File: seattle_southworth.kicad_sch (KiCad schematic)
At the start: 20 parts

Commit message: pier 50 routing checkpoint
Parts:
- added LED1221, LED1222, LED1223: WS2812B-2020, EasyEDA:LED-SMD_4P-L2.0-W2.0-TL_WS2812B-2020, symbol EasyEDA:WS2812B-2020
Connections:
- net +VLED: now also LED1221.4 (VDD), LED1222.4 (VDD), LED1223.4 (VDD)
- net GND: now also LED1221.2 (GND), LED1222.2 (GND), LED1223.2 (GND)
- net at LED1210.1 (DO): now also LED1221.3 (DI)
- net at LED1220.1 (DO): now also LED1222.3 (DI)
- net at LED1201.3 (DI): now also LED1223.1 (DO)

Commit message: single ferry track checkpoint
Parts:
- removed LED1211, LED1212, LED1213, LED1214, LED1215, LED1216, LED1217, LED1218, LED1219, LED1220, LED1222: WS2812B-2020, EasyEDA:LED-SMD_4P-L2.0-W2.0-TL_WS2812B-2020, symbol EasyEDA:WS2812B-2020

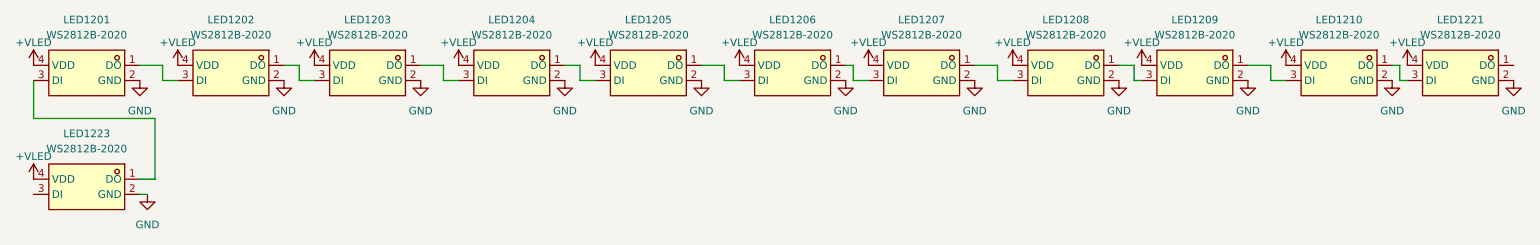
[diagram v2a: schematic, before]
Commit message: Add rail labels
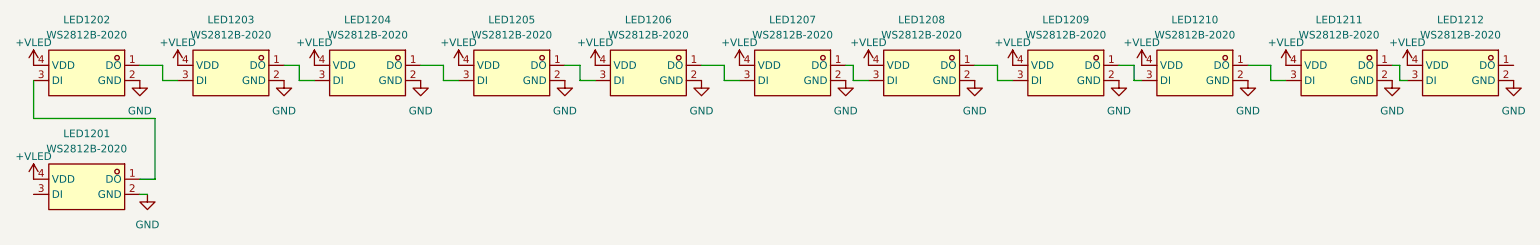
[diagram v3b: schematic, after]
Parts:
- renumbered LED1223 to LED1201, LED1201 to LED1202, LED1202 to LED1203, LED1203 to LED1204, LED1204 to LED1205, LED1205 to LED1206, LED1206 to LED1207, LED1207 to LED1208, LED1208 to LED1209, LED1209 to LED1210, LED1210 to LED1211, LED1221 to LED1212
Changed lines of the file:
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@@
 		(in_pos_files yes)
 		(dnp no)
-		(property "Reference" "LED1204"
+		(property "Reference" "LED1205"
 			(at 109.22 25.4 0)
 			(show_name no)
@@
 			(project "transit"
 				(path "/3763eade-a8c8-4ec0-9cf2-9db4442b4ee5/153adc6e-a3b0-4527-a19a-87e28aab4b4d/7c9fe608-8e01-49b2-89d0-9d6a8f9574e8"
-					(reference "LED1204")
+					(reference "LED1205")
 					(unit 1)
 				)
@@
 		(in_pos_files yes)
 		(dnp no)
-		(property "Reference" "LED1210"
+		(property "Reference" "LED1211"
 			(at 247.65 25.4 0)
 			(show_name no)
@@
 			(project "transit"
 				(path "/3763eade-a8c8-4ec0-9cf2-9db4442b4ee5/153adc6e-a3b0-4527-a19a-87e28aab4b4d/7c9fe608-8e01-49b2-89d0-9d6a8f9574e8"
-					(reference "LED1210")
+					(reference "LED1211")
 					(unit 1)
 				)
@@
 		(in_pos_files yes)
 		(dnp no)
-		(property "Reference" "LED1223"
+		(property "Reference" "LED1201"
 			(at 38.1 44.45 0)
 			(show_name no)
@@
 			(project "transit"
 				(path "/3763eade-a8c8-4ec0-9cf2-9db4442b4ee5/153adc6e-a3b0-4527-a19a-87e28aab4b4d/7c9fe608-8e01-49b2-89d0-9d6a8f9574e8"
-					(reference "LED1223")
+					(reference "LED1201")
 					(unit 1)
 				)
@@
 		(in_pos_files yes)
 		(dnp no)
-		(property "Reference" "LED1208"
+		(property "Reference" "LED1209"
 			(at 201.93 25.4 0)
 			(show_name no)
@@
 			(project "transit"
 				(path "/3763eade-a8c8-4ec0-9cf2-9db4442b4ee5/153adc6e-a3b0-4527-a19a-87e28aab4b4d/7c9fe608-8e01-49b2-89d0-9d6a8f9574e8"
-					(reference "LED1208")
+					(reference "LED1209")
 					(unit 1)
 				)
@@
 		(in_pos_files yes)
 		(dnp no)
-		(property "Reference" "LED1203"
+		(property "Reference" "LED1204"
 			(at 85.09 25.4 0)
 			(show_name no)
@@
 			(project "transit"
 				(path "/3763eade-a8c8-4ec0-9cf2-9db4442b4ee5/153adc6e-a3b0-4527-a19a-87e28aab4b4d/7c9fe608-8e01-49b2-89d0-9d6a8f9574e8"
-					(reference "LED1203")
+					(reference "LED1204")
 					(unit 1)
 				)
@@
 		(in_pos_files yes)
 		(dnp no)
-		(property "Reference" "LED1221"
+		(property "Reference" "LED1212"
 			(at 267.97 25.4 0)
 			(show_name no)
@@
 			(project "transit"
 				(path "/3763eade-a8c8-4ec0-9cf2-9db4442b4ee5/153adc6e-a3b0-4527-a19a-87e28aab4b4d/7c9fe608-8e01-49b2-89d0-9d6a8f9574e8"
-					(reference "LED1221")
+					(reference "LED1212")
 					(unit 1)
 				)
@@
 		(in_pos_files yes)
 		(dnp no)
-		(property "Reference" "LED1206"
+		(property "Reference" "LED1207"
 			(at 156.21 25.4 0)
 			(show_name no)
@@
 			(project "transit"
 				(path "/3763eade-a8c8-4ec0-9cf2-9db4442b4ee5/153adc6e-a3b0-4527-a19a-87e28aab4b4d/7c9fe608-8e01-49b2-89d0-9d6a8f9574e8"
-					(reference "LED1206")
+					(reference "LED1207")
 					(unit 1)
 				)
@@
 		(in_pos_files yes)
 		(dnp no)
-		(property "Reference" "LED1205"
+		(property "Reference" "LED1206"
 			(at 132.08 25.4 0)
 			(show_name no)
@@
 			(project "transit"
 				(path "/3763eade-a8c8-4ec0-9cf2-9db4442b4ee5/153adc6e-a3b0-4527-a19a-87e28aab4b4d/7c9fe608-8e01-49b2-89d0-9d6a8f9574e8"
-					(reference "LED1205")
+					(reference "LED1206")
 					(unit 1)
 				)
@@
 		(in_pos_files yes)
 		(dnp no)
-		(property "Reference" "LED1202"
+		(property "Reference" "LED1203"
 			(at 62.23 25.4 0)
 			(show_name no)
@@
 			(project "transit"
 				(path "/3763eade-a8c8-4ec0-9cf2-9db4442b4ee5/153adc6e-a3b0-4527-a19a-87e28aab4b4d/7c9fe608-8e01-49b2-89d0-9d6a8f9574e8"
-					(reference "LED1202")
+					(reference "LED1203")
 					(unit 1)
 				)
@@
 		(in_pos_files yes)
 		(dnp no)
-		(property "Reference" "LED1209"
+		(property "Reference" "LED1210"
 			(at 223.52 25.4 0)
 			(show_name no)
@@
 			(project "transit"
 				(path "/3763eade-a8c8-4ec0-9cf2-9db4442b4ee5/153adc6e-a3b0-4527-a19a-87e28aab4b4d/7c9fe608-8e01-49b2-89d0-9d6a8f9574e8"
-					(reference "LED1209")
+					(reference "LED1210")
 					(unit 1)
 				)
@@
 		(in_pos_files yes)
 		(dnp no)
-		(property "Reference" "LED1201"
+		(property "Reference" "LED1202"
 			(at 38.1 25.4 0)
 			(show_name no)
@@
 			(project "transit"
 				(path "/3763eade-a8c8-4ec0-9cf2-9db4442b4ee5/153adc6e-a3b0-4527-a19a-87e28aab4b4d/7c9fe608-8e01-49b2-89d0-9d6a8f9574e8"
-					(reference "LED1201")
+					(reference "LED1202")
 					(unit 1)
 				)
@@
 		(in_pos_files yes)
 		(dnp no)
-		(property "Reference" "LED1207"
+		(property "Reference" "LED1208"
 			(at 177.8 25.4 0)
 			(show_name no)
@@
 			(project "transit"
 				(path "/3763eade-a8c8-4ec0-9cf2-9db4442b4ee5/153adc6e-a3b0-4527-a19a-87e28aab4b4d/7c9fe608-8e01-49b2-89d0-9d6a8f9574e8"
-					(reference "LED1207")
-					(unit 1)
-				)
+					(reference "LED1208")
+					(unit 1)
+				)

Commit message: junction checkpoint
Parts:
- added LED1213: WS2812B-2020, EasyEDA:LED-SMD_4P-L2.0-W2.0-TL_WS2812B-2020, symbol EasyEDA:WS2812B-2020
- renumbered LED1212 to LED1201, LED1211 to LED1202, LED1210 to LED1203, LED1209 to LED1204, LED1208 to LED1205, LED1207 to LED1206, LED1206 to LED1207, LED1205 to LED1208, LED1204 to LED1209, LED1203 to LED1210, LED1202 to LED1211, LED1201 to LED1212
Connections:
- net +VLED: now also LED1213.4 (VDD)
- net GND: now also LED1213.2 (GND)
- net at LED1208.1 (DO): now also LED1209.3 (DI); no longer LED1207.3 (DI)
- net at LED1208.3 (DI): now also LED1207.1 (DO); no longer LED1209.1 (DO)
- net at LED1202.1 (DO): now also LED1203.3 (DI); no longer LED1201.3 (DI)
- net at LED1202.3 (DI): now also LED1201.1 (DO); no longer LED1203.1 (DO)
- net at LED1212.1 (DO): now also LED1213.3 (DI); no longer LED1211.3 (DI)
- net at LED1212.3 (DI): now also LED1211.1 (DO)
- net at LED1204.1 (DO): now also LED1205.3 (DI); no longer LED1203.3 (DI)
- net at LED1204.3 (DI): now also LED1203.1 (DO); no longer LED1205.1 (DO)
- net at LED1210.1 (DO): now also LED1211.3 (DI); no longer LED1209.3 (DI)
- net at LED1206.1 (DO): now also LED1207.3 (DI); no longer LED1205.3 (DI)
- net at LED1206.3 (DI): now also LED1205.1 (DO); no longer LED1207.1 (DO)
- net at LED1210.3 (DI): now also LED1209.1 (DO); no longer LED1211.1 (DO)
- new net WATER_TAXI_SOUTHWORTH: LED1201.3 (DI)
- new net WT_FERRY_MERGE: LED1213.1 (DO)
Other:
- moved on the sheet: LED1201, LED1202, LED1203, LED1204, LED1205, LED1206, LED1207, LED1208, LED1209, LED1210, LED1211, LED1212

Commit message: rev-b validation run
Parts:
- LED1201, LED1202, LED1203, LED1204, LED1205, LED1206, LED1207, LED1208, LED1209, LED1210, LED1211, LED1212, LED1213: LCSC Part C965555 -> C52917434
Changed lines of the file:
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@@
 	(generator_version "10.0")
 	(paper "A4")
-	(junction
-		(at 88.265 88.9)
-		(diameter 0)
-		(color 0 0 0 0)
-	)
 	(wire
 		(pts
@@
 	(wire
 		(pts
-			(xy 86.36 88.9) (xy 88.265 88.9)
-		)
-		(stroke
-			(width 0)
-			(type default)
-		)
-	)
-	(wire
-		(pts
 			(xy 190.5 88.265) (xy 190.5 89.535)
 		)
@@
 			)
 		)
-		(property "Datasheet" "https://lcsc.com/product-detail/Light-Emitting-Diodes-LED_Worldsemi-WS2812B-2020_C965555.html"
+		(property "Datasheet" "https://lcsc.com/product-detail/Light-Emitting-Diodes-LED_Worldsemi-WS2812B-2020_C52917434.html"
 			(at 181.61 128.27 0)
 			(hide yes)
@@
 			)
 		)
-		(property "LCSC Part" "C965555"
+		(property "LCSC Part" "C52917434"
 			(at 181.61 130.81 0)
 			(hide yes)
@@
 			)
 		)
-		(property "Datasheet" "https://lcsc.com/product-detail/Light-Emitting-Diodes-LED_Worldsemi-WS2812B-2020_C965555.html"
+		(property "Datasheet" "https://lcsc.com/product-detail/Light-Emitting-Diodes-LED_Worldsemi-WS2812B-2020_C52917434.html"
 			(at 57.785 128.27 0)
 			(hide yes)
@@
 			)
 		)
-		(property "LCSC Part" "C965555"
+		(property "LCSC Part" "C52917434"
 			(at 57.785 130.81 0)
 			(hide yes)
@@
 			)
 		)
-		(property "Datasheet" "https://lcsc.com/product-detail/Light-Emitting-Diodes-LED_Worldsemi-WS2812B-2020_C965555.html"
+		(property "Datasheet" "https://lcsc.com/product-detail/Light-Emitting-Diodes-LED_Worldsemi-WS2812B-2020_C52917434.html"
 			(at 88.265 99.06 0)
 			(hide yes)
@@
 			)
 		)
-		(property "LCSC Part" "C965555"
+		(property "LCSC Part" "C52917434"
 			(at 88.265 101.6 0)
 			(hide yes)
@@
 			)
 		)
-		(property "Datasheet" "https://lcsc.com/product-detail/Light-Emitting-Diodes-LED_Worldsemi-WS2812B-2020_C965555.html"
+		(property "Datasheet" "https://lcsc.com/product-detail/Light-Emitting-Diodes-LED_Worldsemi-WS2812B-2020_C52917434.html"
 			(at 158.115 128.27 0)
 			(hide yes)
@@
 			)
 		)
-		(property "LCSC Part" "C965555"
+		(property "LCSC Part" "C52917434"
 			(at 158.115 130.81 0)
 			(hide yes)
@@
 			)
 		)
-		(property "Datasheet" "https://lcsc.com/product-detail/Light-Emitting-Diodes-LED_Worldsemi-WS2812B-2020_C965555.html"
+		(property "Datasheet" "https://lcsc.com/product-detail/Light-Emitting-Diodes-LED_Worldsemi-WS2812B-2020_C52917434.html"
 			(at 135.255 99.06 0)
 			(hide yes)
@@
 			)
 		)
-		(property "LCSC Part" "C965555"
+		(property "LCSC Part" "C52917434"
 			(at 135.255 101.6 0)
 			(hide yes)
@@
 			)
 		)
-		(property "Datasheet" "https://lcsc.com/product-detail/Light-Emitting-Diodes-LED_Worldsemi-WS2812B-2020_C965555.html"
+		(property "Datasheet" "https://lcsc.com/product-detail/Light-Emitting-Diodes-LED_Worldsemi-WS2812B-2020_C52917434.html"
 			(at 81.915 128.27 0)
 			(hide yes)
@@
 			)
 		)
-		(property "LCSC Part" "C965555"
+		(property "LCSC Part" "C52917434"
 			(at 81.915 130.81 0)
 			(hide yes)
@@
 			)
 		)
-		(property "Datasheet" "https://lcsc.com/product-detail/Light-Emitting-Diodes-LED_Worldsemi-WS2812B-2020_C965555.html"
+		(property "Datasheet" "https://lcsc.com/product-detail/Light-Emitting-Diodes-LED_Worldsemi-WS2812B-2020_C52917434.html"
 			(at 64.135 99.06 0)
 			(hide yes)
@@
 			)
 		)
-		(property "LCSC Part" "C965555"
+		(property "LCSC Part" "C52917434"
 			(at 64.135 101.6 0)
 			(hide yes)
@@
 			)
 		)
-		(property "Datasheet" "https://lcsc.com/product-detail/Light-Emitting-Diodes-LED_Worldsemi-WS2812B-2020_C965555.html"
+		(property "Datasheet" "https://lcsc.com/product-detail/Light-Emitting-Diodes-LED_Worldsemi-WS2812B-2020_C52917434.html"
 			(at 184.785 99.695 0)
 			(hide yes)
@@
 			)
 		)
-		(property "LCSC Part" "C965555"
+		(property "LCSC Part" "C52917434"
 			(at 184.785 102.235 0)
 			(hide yes)
@@
 			)
 		)
-		(property "Datasheet" "https://lcsc.com/product-detail/Light-Emitting-Diodes-LED_Worldsemi-WS2812B-2020_C965555.html"
+		(property "Datasheet" "https://lcsc.com/product-detail/Light-Emitting-Diodes-LED_Worldsemi-WS2812B-2020_C52917434.html"
 			(at 208.28 99.695 0)
 			(hide yes)
@@
 			)
 		)
-		(property "LCSC Part" "C965555"
+		(property "LCSC Part" "C52917434"
 			(at 208.28 102.235 0)
 			(hide yes)
@@
 			)
 		)
-		(property "Datasheet" "https://lcsc.com/product-detail/Light-Emitting-Diodes-LED_Worldsemi-WS2812B-2020_C965555.html"
+		(property "Datasheet" "https://lcsc.com/product-detail/Light-Emitting-Diodes-LED_Worldsemi-WS2812B-2020_C52917434.html"
 			(at 106.68 128.27 0)
 			(hide yes)
@@
 			)
 		)
-		(property "LCSC Part" "C965555"
+		(property "LCSC Part" "C52917434"
 			(at 106.68 130.81 0)
 			(hide yes)
@@
 			)
 		)
-		(property "Datasheet" "https://lcsc.com/product-detail/Light-Emitting-Diodes-LED_Worldsemi-WS2812B-2020_C965555.html"
+		(property "Datasheet" "https://lcsc.com/product-detail/Light-Emitting-Diodes-LED_Worldsemi-WS2812B-2020_C52917434.html"
 			(at 111.125 99.06 0)
 			(hide yes)
@@
 			)
 		)
-		(property "LCSC Part" "C965555"
+		(property "LCSC Part" "C52917434"
 			(at 111.125 101.6 0)
 			(hide yes)
@@
 			)
 		)
-		(property "Datasheet" "https://lcsc.com/product-detail/Light-Emitting-Diodes-LED_Worldsemi-WS2812B-2020_C965555.html"
+		(property "Datasheet" "https://lcsc.com/product-detail/Light-Emitting-Diodes-LED_Worldsemi-WS2812B-2020_C52917434.html"
 			(at 131.445 128.905 0)
 			(hide yes)
@@
 			)
 		)
-		(property "LCSC Part" "C965555"
+		(property "LCSC Part" "C52917434"
 			(at 131.445 131.445 0)
 			(hide yes)
@@
 			)
 		)
-		(property "Datasheet" "https://lcsc.com/product-detail/Light-Emitting-Diodes-LED_Worldsemi-WS2812B-2020_C965555.html"
+		(property "Datasheet" "https://lcsc.com/product-detail/Light-Emitting-Diodes-LED_Worldsemi-WS2812B-2020_C52917434.html"
 			(at 160.02 99.06 0)
 			(hide yes)
@@
 			)
 		)
-		(property "LCSC Part" "C965555"
+		(property "LCSC Part" "C52917434"
 			(at 160.02 101.6 0)
 			(hide yes)
